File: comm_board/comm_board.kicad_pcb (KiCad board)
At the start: 4 copper layers, 80 x 80 mm, 187 parts, among them IC1 CC1101RGPR, J1 RJ45_Amphenol_RJMG1BD3B8K1ANR, J2 PC104 Conn_02x20_Odd_Even, J3 Conn_01x05_Pin Vertical, J4 10155435-00011LF, J5 Conn_01x04_Pin Vertical, J6 SMA Jack, J7 Conn_02x03_Odd_Even, J8 SMA Jack, SW1 EVP-AA602W, SW2 EVP-AA602W, U1 W5500, U10 TPS22968QDMGRQ1, U11 PE4250MLI, U12 MT29F4G01ABAFDWB-IT:F TR, U13 CC1190RGVR, U2 TCAN3414, U3 TCAN3414, U4 MCP23008T-E/SS, U5 INA226AIDGSR, U6 TPS22968QDMGRQ1, U7 STM32L496RGTx, U8 74LVC2G07, U9 MR25H10, X1 25MHz, X2 10MHz, X3 32.768KHZ, Y1 26MHz

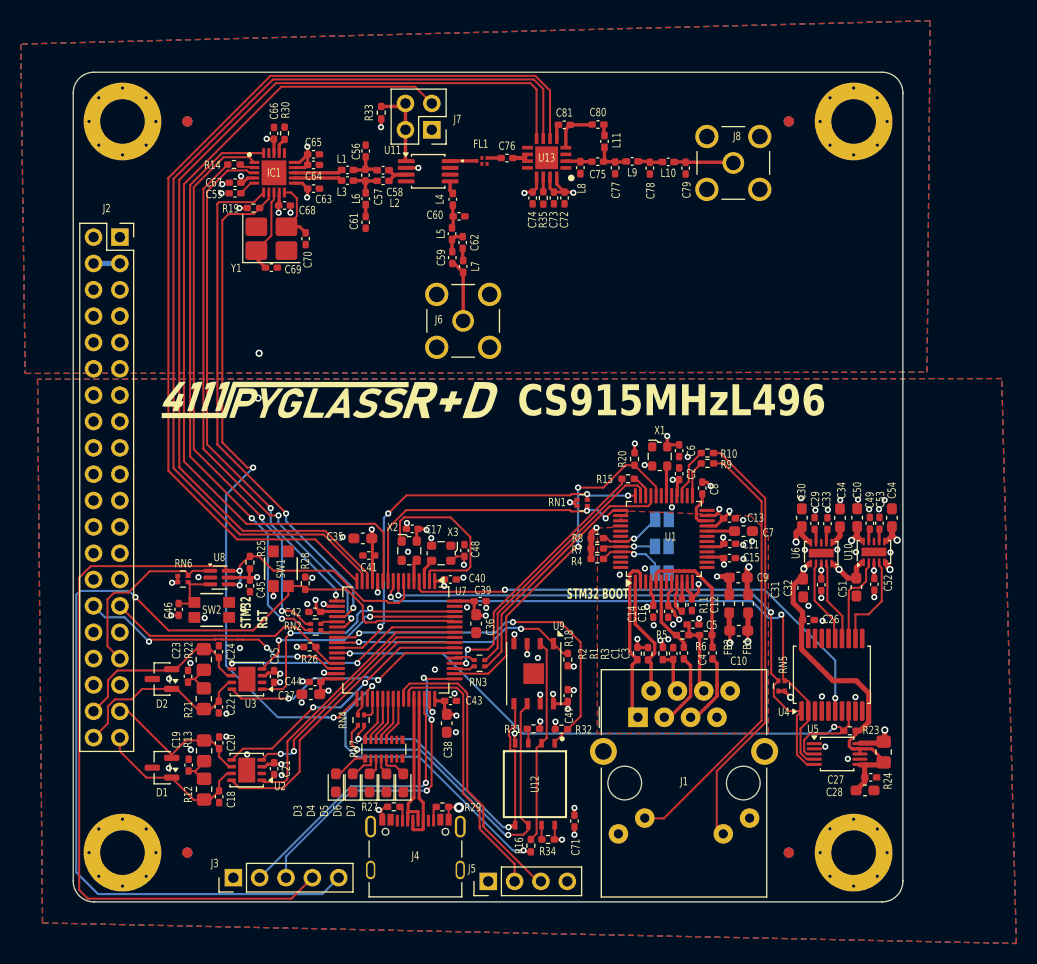
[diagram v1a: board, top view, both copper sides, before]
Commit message: absolute paths for includes of includes or the second level common/sheet will cause problems!
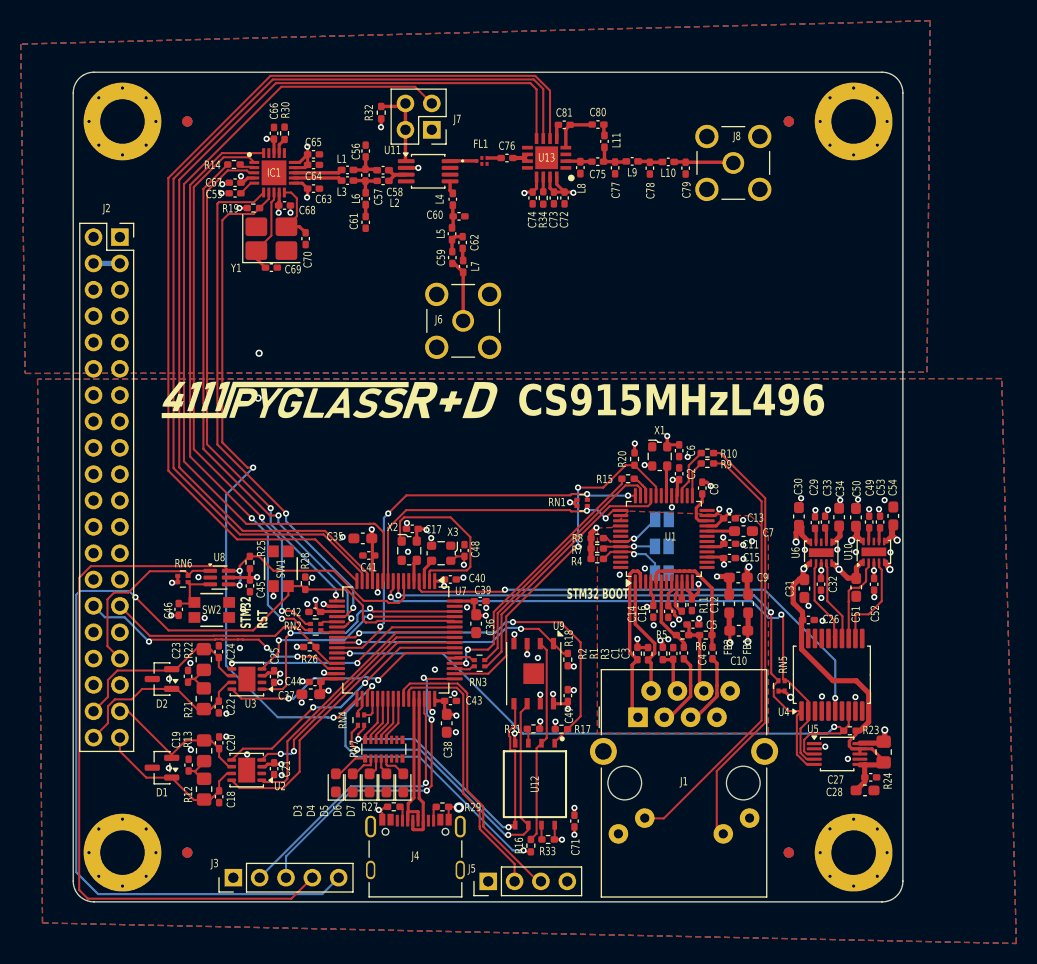
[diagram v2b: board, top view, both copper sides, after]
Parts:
- removed the R32 at (107.1, 123.3)
- added R17: 100K, Resistor_SMD:R_0402_1005Metric_Pad0.72x0.64mm_HandSolder, F.Cu at (107.1, 123.3)
- moved C30 0.30 mm to (130.0, 102.8)
- moved C33 0.27 mm to (132.5, 103.4)
- moved C54 0.22 mm to (139.1, 102.8)
- moved C49 0.13 mm to (136.8, 103.4)
- moved C53 0.13 mm to (137.8, 103.4)
- moved C31 0.13 mm to (130.5, 109.8)
- moved C50 0.12 mm to (135.5, 102.9)
- moved C34 0.11 mm to (133.8, 102.9)
- moved C29 0.09 mm to (131.5, 103.4)
- moved C32 0.06 mm to (132.1, 109.4)
- renumbered FID5 to FID2, FID6 to FID3, FID2 to FID4, FID7 to FID5, FID3 to FID6, FID8 to FID7, FID4 to FID8, R33 to R32, R34 to R33, R35 to R34
